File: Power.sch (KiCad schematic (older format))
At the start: 23 parts, among them J9 GS2, U81 INA181AX, U82 TL1963A-33DCYR, U83 INA181AX, U84 LM2931, U85 INA181AX

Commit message: finished up uC sheet and pressure transducers
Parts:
- removed D33: D, sternie:SOD-128, symbol Device:D
- removed F1: Fuse, Resistors_SMD:R_0603, symbol Device:Fuse
- removed JP3, JP4: Jumper, Pin_Headers:Pin_Header_Straight_1x02_Pitch2.54mm, symbol Device:Jumper
- removed R295: R, Resistors_SMD:R_1206, symbol Device:R
- removed U81: INA181AX, TO_SOT_Packages_SMD:SOT-23-6, symbol engine_controller_series3-rescue:INA181AX-sternie
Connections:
- net labels removed: TRICKLE_IN_N, TRICKLE_IN_P, TRICKLE_OUT_N, TRICKLE_OUT_P, i_charge, vbatt
- wire segments 100 -> 73
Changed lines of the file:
@@
 $Descr A4 11693 8268
 encoding utf-8
-Sheet 2 10
+Sheet 2 11
 Title "Engine Controller Series 3"
 Date ""
@@
 Comment4 ""
 $EndDescr
-Text GLabel 6050 5025 2    49   Input ~ 0
-vbatt
 $Comp
 L engine_controller_series3-rescue:TL1963A-33DCYR-sternie U82
@@
 	1    0    0    -1
 $EndComp
-$Comp
-L Device:D D33
-U 1 1 5ABE5BD3
-P 5350 5025
-F 0 "D33" H 5350 5125 50  0000 C CNN
-F 1 "D" H 5350 4925 50  0000 C CNN
-F 2 "sternie:SOD-128" H 5350 5025 50  0001 C CNN
-F 3 "" H 5350 5025 50  0001 C CNN
-	1    5350 5025
-	-1   0    0    1
-$EndComp
-Text GLabel 4000 5025 0    49   Input ~ 0
-TRICKLE_IN_P
-Text GLabel 4075 5975 0    49   Input ~ 0
-TRICKLE_IN_N
-Text GLabel 5200 5400 2    49   Input ~ 0
-TRICKLE_OUT_P
-Text GLabel 4225 5975 2    49   Input ~ 0
-TRICKLE_OUT_N
-$Comp
-L Device:Jumper JP3
-U 1 1 5ABE5BDE
-P 4800 5025
-AR Path="/5972C978/5ABE5BDE" Ref="JP3"  Part="1"
-AR Path="/5966DBAF/5968371C/5ABE5BDE" Ref="JP?"  Part="1"
-AR Path="/5E49E7E9/5ABE5BDE" Ref="JP3"  Part="1"
-F 0 "JP3" H 4800 5175 50  0000 C CNN
-F 1 "Jumper" H 4800 4945 50  0000 C CNN
-F 2 "Pin_Headers:Pin_Header_Straight_1x02_Pitch2.54mm" H 4800 5025 50  0001 C CNN
-F 3 "" H 4800 5025 50  0001 C CNN
-	1    4800 5025
-	1    0    0    -1
-$EndComp
-$Comp
-L Device:Jumper JP4
-U 1 1 5ABE5BE5
-P 4800 5400
-F 0 "JP4" H 4800 5550 50  0000 C CNN
-F 1 "Jumper" H 4800 5320 50  0000 C CNN
-F 2 "Pin_Headers:Pin_Header_Straight_1x02_Pitch2.54mm" H 4800 5400 50  0001 C CNN
-F 3 "" H 4800 5400 50  0001 C CNN
-	1    4800 5400
-	1    0    0    -1
-$EndComp
-$Comp
-L Device:Fuse F1
-U 1 1 5ABE5BEC
-P 4250 5025
-F 0 "F1" V 4330 5025 50  0000 C CNN
-F 1 "Fuse" V 4175 5025 50  0000 C CNN
-F 2 "Resistors_SMD:R_0603" V 4180 5025 50  0001 C CNN
-F 3 "" H 4250 5025 50  0001 C CNN
-	1    4250 5025
-	0    1    1    0
-$EndComp
-Wire Wire Line
-	4000 5025 4100 5025
-Wire Wire Line
-	4400 5025 4450 5025
-Wire Wire Line
-	4500 5400 4450 5400
-Wire Wire Line
-	4450 5400 4450 5025
-Connection ~ 4450 5025
-Wire Wire Line
-	5100 5025 5200 5025
-Wire Wire Line
-	5100 5400 5200 5400
-Wire Wire Line
-	4075 5975 4150 5975
 Wire Wire Line
 	4150 5975 4150 6025
-Connection ~ 4150 5975
-$Comp
-L engine_controller_series3-rescue:INA181AX-sternie U81
-U 1 1 5ABE80DE
-P 5750 4425
-F 0 "U81" H 5750 4675 49  0000 C CNN
-F 1 "INA181AX" H 5700 4175 49  0000 C CNN
-F 2 "TO_SOT_Packages_SMD:SOT-23-6" H 5300 4725 49  0001 C CNN
-F 3 "" H 5300 4725 49  0001 C CNN
-	1    5750 4425
-	1    0    0    -1
-$EndComp
-$Comp
-L Device:R R295
-U 1 1 5ABE81FE
-P 5750 5025
-F 0 "R295" V 5830 5025 50  0000 C CNN
-F 1 "R" V 5750 5025 50  0000 C CNN
-F 2 "Resistors_SMD:R_1206" V 5680 5025 50  0001 C CNN
-F 3 "" H 5750 5025 50  0001 C CNN
-	1    5750 5025
-	0    1    1    0
-$EndComp
-Wire Wire Line
-	5500 5025 5550 5025
-Wire Wire Line
-	5300 4525 5225 4525
-Wire Wire Line
-	5225 4525 5225 4825
-Wire Wire Line
-	5225 4825 5550 4825
-Wire Wire Line
-	5550 4825 5550 5025
-Connection ~ 5550 5025
-Wire Wire Line
-	6150 4525 6225 4525
-Wire Wire Line
-	6225 4525 6225 4900
-Wire Wire Line
-	6225 4900 5950 4900
-Wire Wire Line
-	5950 4900 5950 5025
-Wire Wire Line
-	5900 5025 5950 5025
-$Comp
-L power:+3.3V #PWR0622
-U 1 1 5ABE95EA
-P 6225 4200
-F 0 "#PWR0622" H 6225 4050 50  0001 C CNN
-F 1 "+3.3V" H 6225 4340 50  0000 C CNN
-F 2 "" H 6225 4200 50  0001 C CNN
-F 3 "" H 6225 4200 50  0001 C CNN
-	1    6225 4200
-	1    0    0    -1
-$EndComp
-Wire Wire Line
-	6150 4325 6225 4325
-Wire Wire Line
-	6225 4325 6225 4200
-$Comp
-L power:GND #PWR0617
-U 1 1 5ABE96BB
-P 5075 4550
-F 0 "#PWR0617" H 5075 4300 50  0001 C CNN
-F 1 "GND" H 5075 4400 50  0000 C CNN
-F 2 "" H 5075 4550 50  0001 C CNN
-F 3 "" H 5075 4550 50  0001 C CNN
-	1    5075 4550
-	1    0    0    -1
-$EndComp
-Wire Wire Line
-	5300 4425 5075 4425
-Wire Wire Line
-	5075 4425 5075 4550
-$Comp
-L power:GND #PWR0623
-U 1 1 5ABE97A8
-P 6350 4525
-F 0 "#PWR0623" H 6350 4275 50  0001 C CNN
-F 1 "GND" H 6350 4375 50  0000 C CNN
-F 2 "" H 6350 4525 50  0001 C CNN
-F 3 "" H 6350 4525 50  0001 C CNN
-	1    6350 4525
-	1    0    0    -1
-$EndComp
-Wire Wire Line
-	6150 4425 6350 4425
-Wire Wire Line
-	6350 4425 6350 4525
-Text GLabel 5300 4325 0    49   Input ~ 0
-i_charge
-Connection ~ 5950 5025
 Text GLabel 4150 5975 1    49   Input ~ 0
 GNDPWR
@@
 	8300 2575 8375 2575
 Wire Wire Line
-	4450 5025 4500 5025
-Wire Wire Line
-	4150 5975 4225 5975
-Wire Wire Line
-	5550 5025 5600 5025
-Wire Wire Line
-	5950 5025 6050 5025
-Wire Wire Line
 	7775 2675 8300 2675

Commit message: Valves and ducers
Finished valves and ducers and their connectors. Got rid of 4 pin ducers. Made all ducers powered by +5V. Cleaned up some uneeded files.
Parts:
- U82, U84: symbol engine_controller_series3-rescue:TL1963A-33DCYR-sternie -> bangbang_rev1-rescue:TL1963A-33DCYR-sternie-engine_controller_series3-rescue
- U83, U85: symbol engine_controller_series3-rescue:INA181AX-sternie -> bangbang_rev1-rescue:INA181AX-sternie-engine_controller_series3-rescue
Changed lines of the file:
@@
 $EndDescr
 $Comp
-L engine_controller_series3-rescue:TL1963A-33DCYR-sternie U82
+L bangbang_rev1-rescue:TL1963A-33DCYR-sternie-engine_controller_series3-rescue U82
 U 1 1 5972DA06
 P 4725 2225
@@
 $EndComp
 $Comp
-L engine_controller_series3-rescue:TL1963A-33DCYR-sternie U84
+L bangbang_rev1-rescue:TL1963A-33DCYR-sternie-engine_controller_series3-rescue U84
 U 1 1 597518BD
 P 8325 2125
@@
 	8300 2675 8850 2675
 $Comp
-L engine_controller_series3-rescue:INA181AX-sternie U83
+L bangbang_rev1-rescue:INA181AX-sternie-engine_controller_series3-rescue U83
 U 1 1 5BE8BA42
 P 5775 1350
@@
 Connection ~ 4200 2225
 $Comp
-L engine_controller_series3-rescue:INA181AX-sternie U85
+L bangbang_rev1-rescue:INA181AX-sternie-engine_controller_series3-rescue U85
 U 1 1 5BEB6FDF
 P 9375 1250

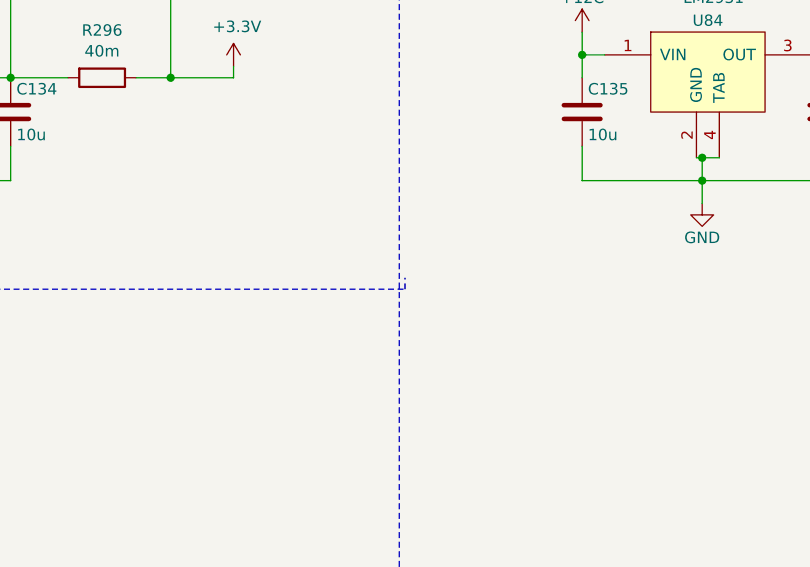
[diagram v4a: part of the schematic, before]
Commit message: Updated Motor Channels
Each motor only needs two inputs.
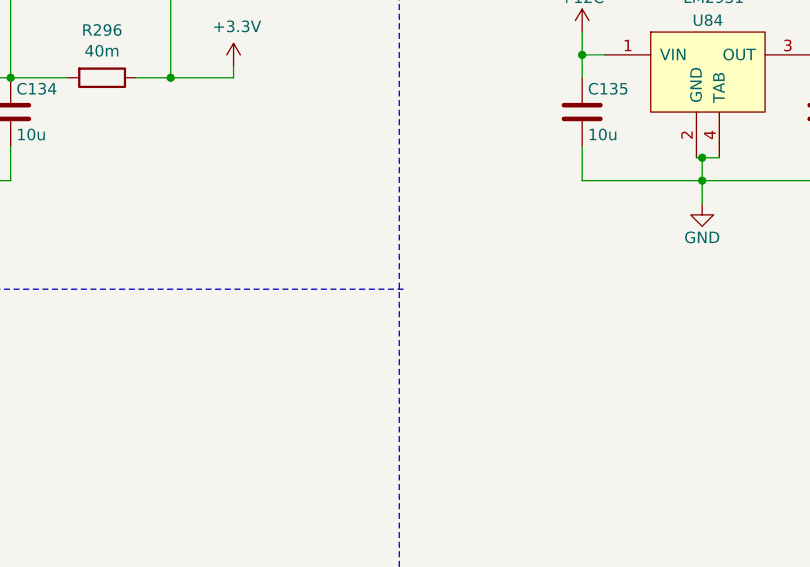
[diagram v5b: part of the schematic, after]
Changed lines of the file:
@@
 Wire Notes Line
 	3650 3150 7000 3150
-Wire Notes Line
-	7000 3150 7000 3100
 $EndSCHEMATC
